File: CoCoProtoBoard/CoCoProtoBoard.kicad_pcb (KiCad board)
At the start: 2 copper layers, 100 x 96 mm, 833 parts, among them P1 CocoEdgeConnector, P10 Power Bus, P2 Coco Data, P3 Coco Address, P4 Coco Signals

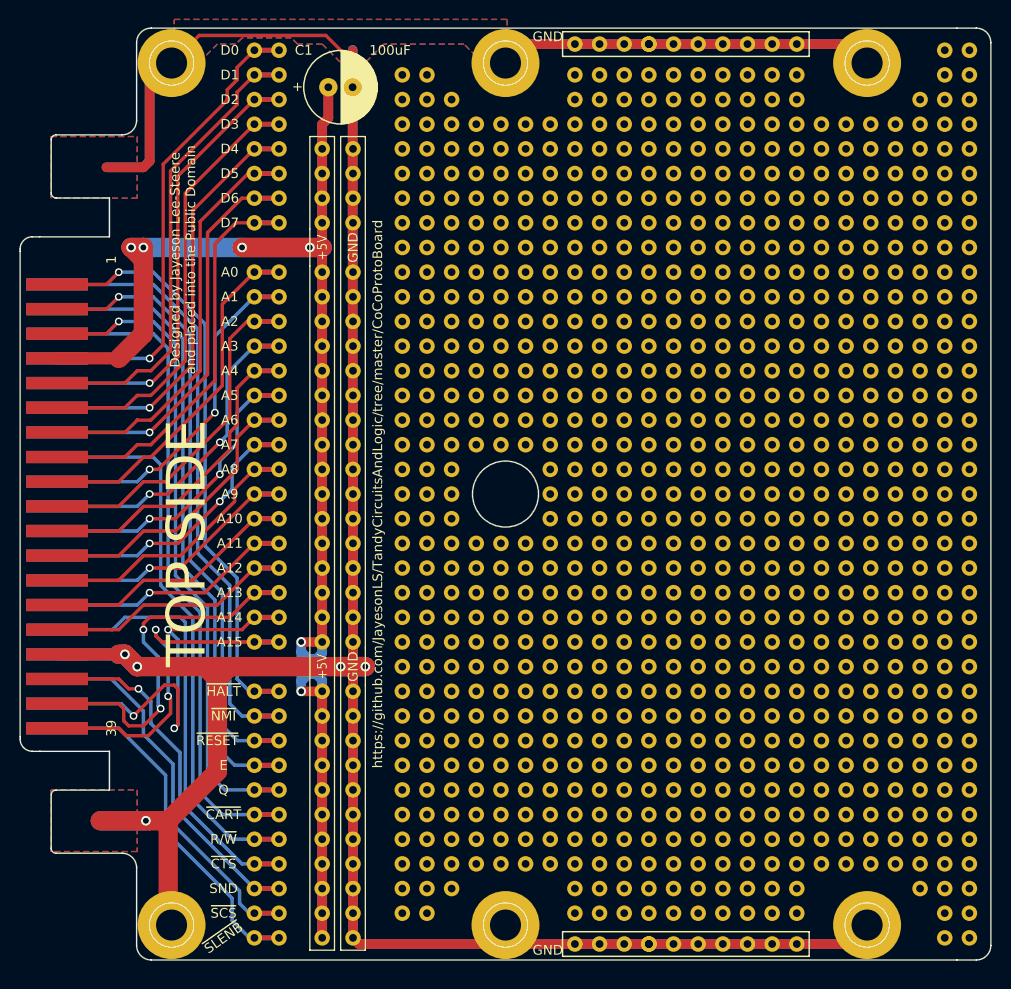
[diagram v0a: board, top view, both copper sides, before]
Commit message: CocoProtoBoard: Swap +5v and GND rails and other minor tweaks.
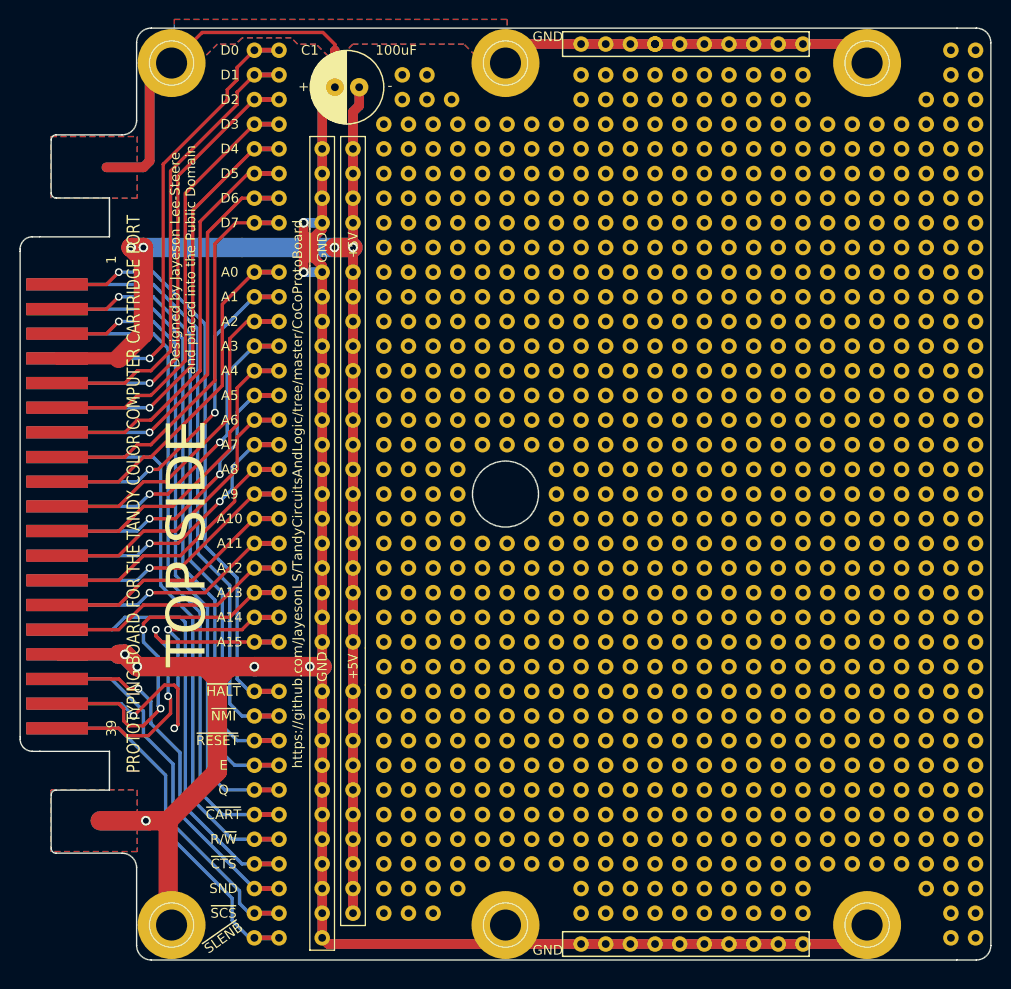
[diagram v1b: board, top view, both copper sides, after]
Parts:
- removed the REF** at (162.6, 150.5)
- removed the REF** at (152.4, 150.5)
- removed the REF** at (147.3, 150.5)
- removed the REF** at (149.9, 150.5)
- removed the REF** at (165.1, 150.5)
- removed the REF** at (154.9, 150.5) (x2)
- removed the REF** at (157.5, 150.5)
- removed the REF** at (160.0, 150.5)
- added REF**: 1pin, Connect:1pin, F.Cu at (148.0, 150.5)
- added REF**: 1pin, Connect:1pin, F.Cu at (128.9, 119.4)
- added REF**: 1pin, Connect:1pin, F.Cu at (128.9, 116.8)
- added REF**: 1pin, Connect:1pin, F.Cu at (128.9, 114.3)
- added REF**: 1pin, Connect:1pin, F.Cu at (128.9, 121.9)
- added REF**: 1pin, Connect:1pin, F.Cu at (128.9, 76.2)
- added REF**: 1pin, Connect:1pin, F.Cu at (128.9, 91.4)
- added REF**: 1pin, Connect:1pin, F.Cu at (128.9, 73.7)
- added REF**: 1pin, Connect:1pin, F.Cu at (128.9, 83.8)
- added REF**: 1pin, Connect:1pin, F.Cu at (128.9, 71.1)
- added REF**: 1pin, Connect:1pin, F.Cu at (128.9, 96.5)
- added REF**: 1pin, Connect:1pin, F.Cu at (150.5, 150.5)
- added REF**: 1pin, Connect:1pin, F.Cu at (128.9, 99.1)
- added REF**: 1pin, Connect:1pin, F.Cu at (128.9, 94.0)
- added REF**: 1pin, Connect:1pin, F.Cu at (128.9, 132.1)
- added REF**: 1pin, Connect:1pin, F.Cu at (128.9, 129.5)
- added REF**: 1pin, Connect:1pin, F.Cu at (128.9, 127.0)
- added REF**: 1pin, Connect:1pin, F.Cu at (128.9, 124.5)
- added REF**: 1pin, Connect:1pin, F.Cu at (128.9, 88.9)
- added REF**: 1pin, Connect:1pin, F.Cu at (128.9, 86.4)
- added REF**: 1pin, Connect:1pin, F.Cu at (128.9, 66.0)
- added REF**: 1pin, Connect:1pin, F.Cu at (128.9, 134.6)
- added REF**: 1pin, Connect:1pin, F.Cu at (153.0, 150.5)
- added REF**: 1pin, Connect:1pin, F.Cu at (128.9, 142.2)
- added REF**: 1pin, Connect:1pin, F.Cu at (128.9, 147.3)
- added REF**: 1pin, Connect:1pin, F.Cu at (128.9, 139.7)
- added REF**: 1pin, Connect:1pin, F.Cu at (128.9, 137.2)
- added REF**: 1pin, Connect:1pin, F.Cu at (128.9, 144.8)
- added REF**: 1pin, Connect:1pin, F.Cu at (128.9, 68.6)
- added REF**: 1pin, Connect:1pin, F.Cu at (128.9, 111.8)
- added REF**: 1pin, Connect:1pin, F.Cu at (128.9, 109.2)
- added REF**: 1pin, Connect:1pin, F.Cu at (128.9, 106.7)
- added REF**: 1pin, Connect:1pin, F.Cu at (128.9, 101.6)
- added REF**: 1pin, Connect:1pin, F.Cu at (155.6, 150.5)
- added REF**: 1pin, Connect:1pin, F.Cu at (128.9, 104.1)
- added REF**: 1pin, Connect:1pin, F.Cu at (128.9, 81.3)
- added REF**: 1pin, Connect:1pin, F.Cu at (160.7, 150.5)
- added REF**: 1pin, Connect:1pin, F.Cu at (158.1, 150.5)
- added REF**: 1pin, Connect:1pin, F.Cu at (163.2, 150.5)
- added REF**: 1pin, Connect:1pin, F.Cu at (165.7, 150.5)
- added REF**: 1pin, Connect:1pin, F.Cu at (128.9, 78.7)
- moved C1 3.17 mm to (126.4, 62.2), turned to 180 degrees
- moved REF** 0.64 mm to (179.7, 66.0)
- moved REF** 0.64 mm to (134.0, 66.0)
- moved REF** 0.64 mm to (144.1, 66.0)
- moved REF** 0.64 mm to (154.3, 66.0)
- moved REF** 0.64 mm to (179.7, 86.4)
- moved REF** 0.64 mm to (144.1, 86.4)
- moved REF** 0.64 mm to (189.9, 86.4)
- moved REF** 0.64 mm to (161.9, 86.4)
- moved REF** 0.64 mm to (134.0, 86.4)
- moved REF** 0.64 mm to (172.1, 88.9)
- moved REF** 0.64 mm to (144.1, 88.9)
- moved REF** 0.64 mm to (161.9, 88.9)
- moved REF** 0.64 mm to (134.0, 96.5)
- moved REF** 0.64 mm to (172.1, 86.4)
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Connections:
- P10 pad 1: +5V -> GND
- P10 pad 2: GND -> +5V
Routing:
- net +5V: track 238.1 -> 222.4 mm, vias 6 -> 4
- net GND: track 522.7 -> 538.3 mm, vias 5 -> 7
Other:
- board text added: "-"
- board text added: "PROTOTYPING BOARD FOR THE TANDY COLOR COMPUTER CARTRIDGE PORT"
